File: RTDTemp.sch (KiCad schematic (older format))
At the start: 100 parts, among them J1 Conn_01x02, J10 Conn_01x02, J11 Conn_01x02, J2 Conn_01x02, J3 Conn_01x02, J4 CAN_In, J5 CAN_Out, J6 Conn_01x02, J7 Conn_01x02, J8 Conn_01x02, J9 Conn_01x02, U1 INA21x, U10 INA21x, U11 INA21x, U12 INA21x, U2 Nucleo_L432KC, U3 PDS1-Sx-Sx, U4 INA21x, U5 ADM3055E, U6 INA21x, U7 CDSOT23-T24CAN, U8 INA21x, U9 INA21x

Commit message: replacedOpAmpswithMaximChip
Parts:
- removed C1, C17, C18, C19, C2, C3, C4, C5: .1u, Capacitor_SMD:C_0805_2012Metric, symbol Device:C
- removed J1, J10, J2, J3, J6, J7, J8, J9: Conn_01x02, Connector_Molex:Molex_Micro-Fit_3.0_43650-0200_1x02_P3.00mm_Horizontal, symbol Connector_Generic:Conn_01x02
- removed R1, R11, R17, R18, R2, R23, R24, R27, R28, R3, R30, R31, R4, R5, R6, R8: 3.3k, Resistor_SMD:R_0805_2012Metric, symbol Device:R
- removed R12, R13, R15, R16, R19, R26, R29, R32: 100, Resistor_SMD:R_0805_2012Metric, symbol Device:R
- removed TP1, TP2, TP3, TP4, TP5, TP6, TP7, TP8: TestPoint, TestPoint:TestPoint_Keystone_5005-5009_Compact, symbol Connector:TestPoint
- removed U1, U10, U11, U12, U4, U6, U8, U9: INA21x, UTSVT_ICs:SOIC-6_1.40x2.15mm_Pitch0.65mm, symbol RTDTemp-rescue:INA21x-MPPT-rescue
- added C1, C17, C18, C19, C2, C20, C23, C24, C25, C26, C29, C3, C30, C31, C32, C4: 100nF, Capacitor_SMD:C_0805_2012Metric, symbol Device:C_Small
- added C21, C22, C27, C28, C33, C34, C5, C8: Ci, Capacitor_SMD:C_0805_2012Metric, symbol Device:C_Small
- added J1, J10, J2, J3, J6, J7, J8, J9: Conn_01x04, Connector_Molex:Molex_Micro-Fit_3.0_43650-0415_1x04_P3.00mm_Vertical, symbol Connector_Generic:Conn_01x04
- added R1, R2, R3, R4, R5, R6, R7, R8: 400, Resistor_SMD:R_0805_2012Metric, symbol Device:R_Small
- added U1, U10, U11, U12, U4, U6, U8, U9: MAX31865xAP, Package_SO:SSOP-20_5.3x7.2mm_P0.65mm, symbol Sensor_Temperature:MAX31865xAP
- U3: symbol utsvt-power-regulators:PDS1-Sx-Sx -> RTDTemp-rescue:PDS1-Sx-Sx-utsvt-power-regulators
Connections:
- net labels added: +3V3, CLK, CS_0, CS_1, CS_2, CS_3, CS_4, CS_5, CS_6, CS_7, DRDY, SDI, SDO
- net labels removed: RTD0, RTD1, RTD2, RTD3, RTD4, RTD5, RTD6, RTD7
- wire segments 309 -> 389
- no-connect marks 19 -> 15
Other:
- moved on the sheet: C10, C11, C12, C13, C14, C15, C16, C6, C7, C9, H1, H2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

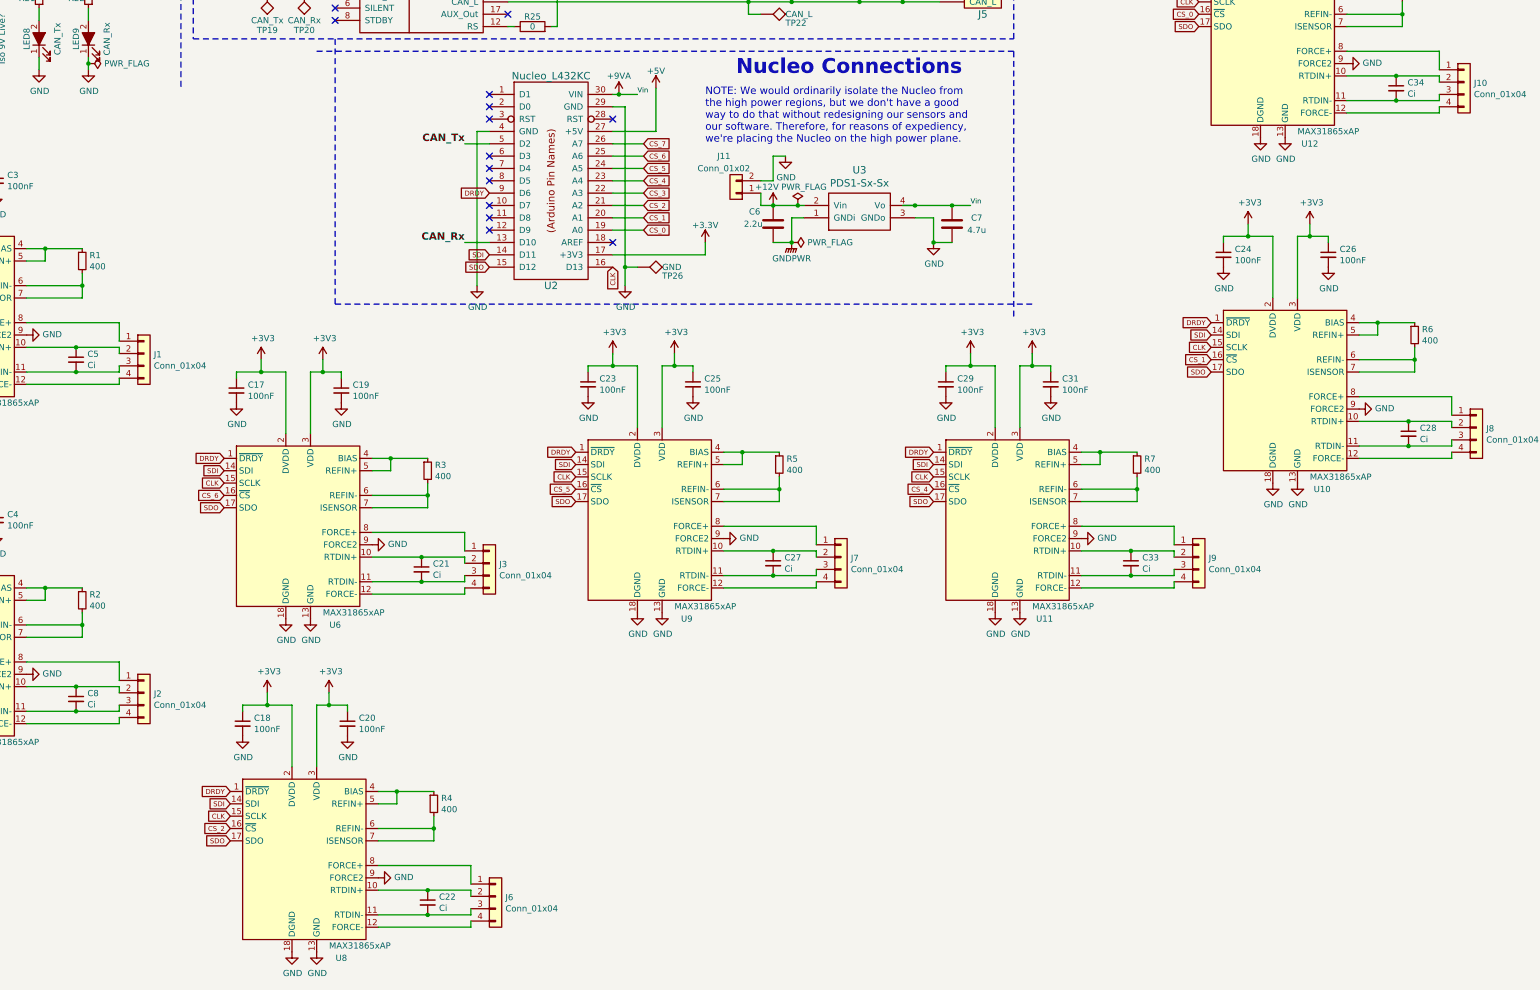
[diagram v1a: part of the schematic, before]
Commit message: Started RTD board layout update
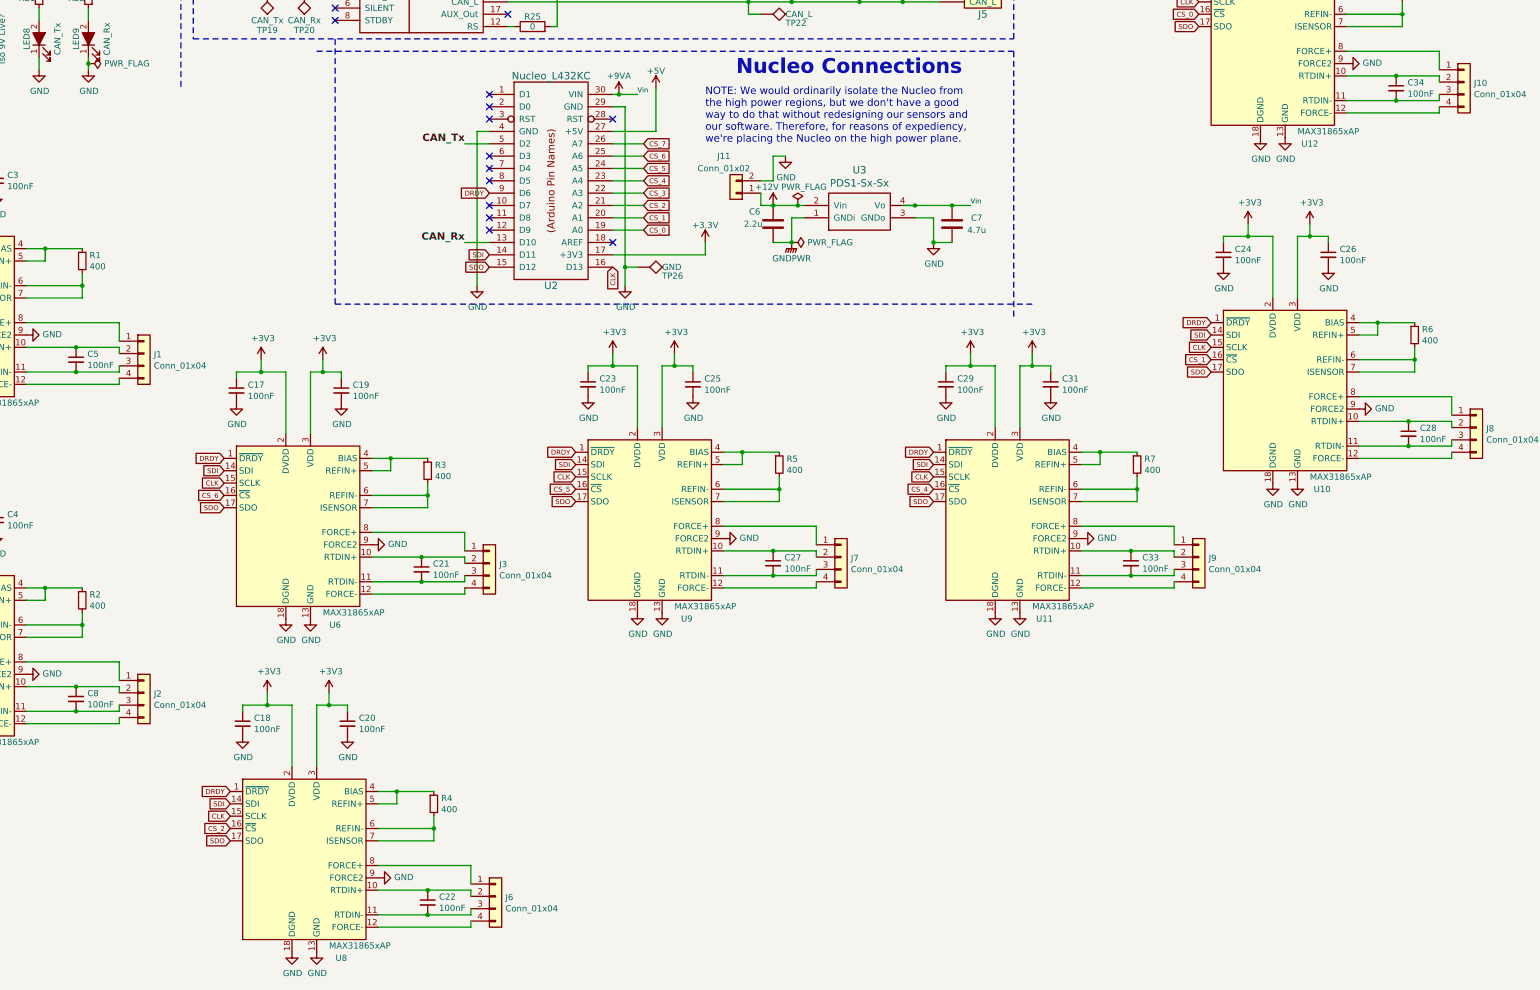
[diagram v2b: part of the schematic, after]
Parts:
- C21, C22, C27, C28, C33, C34, C5, C8: value Ci -> 100nF
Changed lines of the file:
@@
 Wire Wire Line
 	1000 3200 1000 3250
-$Comp
-L Device:C_Small C5
-U 1 1 5FC107A3
-P 2500 4800
-F 0 "C5" H 2592 4846 50  0000 L CNN
-F 1 "Ci" H 2592 4755 50  0000 L CNN
-F 2 "Capacitor_SMD:C_0805_2012Metric" H 2500 4800 50  0001 C CNN
-F 3 "~" H 2500 4800 50  0001 C CNN
-	1    2500 4800
-	1    0    0    -1
-$EndComp
 Wire Wire Line
 	2100 4700 2500 4700
@@
 P 5300 6500
 F 0 "C21" H 5392 6546 50  0000 L CNN
-F 1 "Ci" H 5392 6455 50  0000 L CNN
+F 1 "100nF" H 5392 6455 50  0000 L CNN
 F 2 "Capacitor_SMD:C_0805_2012Metric" H 5300 6500 50  0001 C CNN
 F 3 "~" H 5300 6500 50  0001 C CNN
@@
 P 8150 6450
 F 0 "C27" H 8242 6496 50  0000 L CNN
-F 1 "Ci" H 8242 6405 50  0000 L CNN
+F 1 "100nF" H 8242 6405 50  0000 L CNN
 F 2 "Capacitor_SMD:C_0805_2012Metric" H 8150 6450 50  0001 C CNN
 F 3 "~" H 8150 6450 50  0001 C CNN
@@
 P 11050 6450
 F 0 "C33" H 11142 6496 50  0000 L CNN
-F 1 "Ci" H 11142 6405 50  0000 L CNN
+F 1 "100nF" H 11142 6405 50  0000 L CNN
 F 2 "Capacitor_SMD:C_0805_2012Metric" H 11050 6450 50  0001 C CNN
 F 3 "~" H 11050 6450 50  0001 C CNN
@@
 P 2500 7550
 F 0 "C8" H 2592 7596 50  0000 L CNN
-F 1 "Ci" H 2592 7505 50  0000 L CNN
+F 1 "100nF" H 2592 7505 50  0000 L CNN
 F 2 "Capacitor_SMD:C_0805_2012Metric" H 2500 7550 50  0001 C CNN
 F 3 "~" H 2500 7550 50  0001 C CNN
@@
 P 5350 9200
 F 0 "C22" H 5442 9246 50  0000 L CNN
-F 1 "Ci" H 5442 9155 50  0000 L CNN
+F 1 "100nF" H 5442 9155 50  0000 L CNN
 F 2 "Capacitor_SMD:C_0805_2012Metric" H 5350 9200 50  0001 C CNN
 F 3 "~" H 5350 9200 50  0001 C CNN
@@
 P 13300 5400
 F 0 "C28" H 13392 5446 50  0000 L CNN
-F 1 "Ci" H 13392 5355 50  0000 L CNN
+F 1 "100nF" H 13392 5355 50  0000 L CNN
 F 2 "Capacitor_SMD:C_0805_2012Metric" H 13300 5400 50  0001 C CNN
 F 3 "~" H 13300 5400 50  0001 C CNN
@@
 P 13200 2600
 F 0 "C34" H 13292 2646 50  0000 L CNN
-F 1 "Ci" H 13292 2555 50  0000 L CNN
+F 1 "100nF" H 13292 2555 50  0000 L CNN
 F 2 "Capacitor_SMD:C_0805_2012Metric" H 13200 2600 50  0001 C CNN
 F 3 "~" H 13200 2600 50  0001 C CNN
@@
 	-1   0    0    -1
 $EndComp
+$Comp
+L Device:C_Small C5
+U 1 1 5FC107A3
+P 2500 4800
+F 0 "C5" H 2592 4846 50  0000 L CNN
+F 1 "100nF" H 2592 4755 50  0000 L CNN
+F 2 "Capacitor_SMD:C_0805_2012Metric" H 2500 4800 50  0001 C CNN
+F 3 "~" H 2500 4800 50  0001 C CNN
+	1    2500 4800
+	1    0    0    -1
+$EndComp
 $EndSCHEMATC

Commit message: reset references for rtd specific components, preliminary layout of half of the RTD subcircuits
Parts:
- removed C1, C17, C18, C19, C2, C20, C21, C22, C23, C25, C27, C29, C3, C31, C33, C4, C5, C8: 100nF, Capacitor_SMD:C_0805_2012Metric, symbol Device:C_Small
- removed J1, J2, J3, J6, J7, J9: Conn_01x04, Connector_Molex:Molex_Micro-Fit_3.0_43650-0415_1x04_P3.00mm_Vertical, symbol Connector_Generic:Conn_01x04
- removed R1, R2, R3, R4, R5, R7: 400, Resistor_SMD:R_0805_2012Metric, symbol Device:R_Small
- removed U1, U11, U4, U6, U8, U9: MAX31865xAP, Package_SO:SSOP-20_5.3x7.2mm_P0.65mm, symbol Sensor_Temperature:MAX31865xAP
- added RTD2_C0, RTD2_C1, RTD2_C2, RTD3_C0, RTD3_C1, RTD3_C2, RTD4_C0, RTD4_C1, RTD4_C2, RTD5_C0, RTD5_C1, RTD5_C2, RTD6_C0, RTD6_C1, RTD6_C2, RTD7_C0, RTD7_C1, RTD7_C2: 100nF, Capacitor_SMD:C_0805_2012Metric, symbol Device:C_Small
- added RTD2_J0, RTD3_J0, RTD4_J0, RTD5_J0, RTD6_J0, RTD7_J0: Conn_01x04, Connector_Molex:Molex_Micro-Fit_3.0_43650-0415_1x04_P3.00mm_Vertical, symbol Connector_Generic:Conn_01x04
- added RTD2_R0, RTD3_R0, RTD4_R0, RTD5_R0, RTD6_R0, RTD7_R0: 400, Resistor_SMD:R_0805_2012Metric, symbol Device:R_Small
- added RTD2_U0, RTD3_U0, RTD4_U0, RTD5_U0, RTD6_U0, RTD7_U0: MAX31865xAP, Package_SO:SSOP-20_5.3x7.2mm_P0.65mm, symbol Sensor_Temperature:MAX31865xAP
- renumbered C30 to RTD0_C0, C32 to RTD0_C1, C34 to RTD0_C2, J10 to RTD0_J0, R8 to RTD0_R0, U12 to RTD0_U0, C24 to RTD1_C0, C26 to RTD1_C1, C28 to RTD1_C2, J8 to RTD1_J0, R6 to RTD1_R0, U10 to RTD1_U0
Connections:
- net +3V3: now also RTD2_C0.1, RTD2_C1.1, RTD2_U0.2 (DVDD), RTD2_U0.3 (VDD), RTD3_C0.1, RTD3_C1.1, RTD3_U0.2 (DVDD), RTD3_U0.3 (VDD), RTD4_C0.1, RTD4_C1.1, RTD4_U0.2 (DVDD), RTD4_U0.3 (VDD), RTD5_C0.1, RTD5_C1.1, RTD5_U0.2 (DVDD), RTD5_U0.3 (VDD), RTD6_C0.1, RTD6_C1.1, RTD6_U0.2 (DVDD), RTD6_U0.3 (VDD), RTD7_C0.1, RTD7_C1.1, RTD7_U0.2 (DVDD), RTD7_U0.3 (VDD)
- net CLK: now also RTD2_U0.15 (SCLK), RTD3_U0.15 (SCLK), RTD4_U0.15 (SCLK), RTD5_U0.15 (SCLK), RTD6_U0.15 (SCLK), RTD7_U0.15 (SCLK)
- net CS_2: now also RTD2_U0.16 (~CS)
- net CS_3: now also RTD3_U0.16 (~CS)
- net CS_4: now also RTD4_U0.16 (~CS)
- net CS_5: now also RTD5_U0.16 (~CS)
- net CS_6: now also RTD6_U0.16 (~CS)
- net CS_7: now also RTD7_U0.16 (~CS)
- net DRDY: now also RTD2_U0.1 (~DRDY), RTD3_U0.1 (~DRDY), RTD4_U0.1 (~DRDY), RTD5_U0.1 (~DRDY), RTD6_U0.1 (~DRDY), RTD7_U0.1 (~DRDY)
- net GND: now also RTD2_C0.2, RTD2_C1.2, RTD2_U0.13 (GND), RTD2_U0.18 (DGND), RTD2_U0.19 (GND), RTD2_U0.9 (FORCE2), RTD3_C0.2, RTD3_C1.2, RTD3_U0.13 (GND), RTD3_U0.18 (DGND), RTD3_U0.19 (GND), RTD3_U0.9 (FORCE2), RTD4_C0.2, RTD4_C1.2, RTD4_U0.13 (GND), RTD4_U0.18 (DGND), RTD4_U0.19 (GND), RTD4_U0.9 (FORCE2), RTD5_C0.2, RTD5_C1.2, RTD5_U0.13 (GND), RTD5_U0.18 (DGND), RTD5_U0.19 (GND), RTD5_U0.9 (FORCE2), RTD6_C0.2, RTD6_C1.2, RTD6_U0.13 (GND), RTD6_U0.18 (DGND), RTD6_U0.19 (GND), RTD6_U0.9 (FORCE2), RTD7_C0.2, RTD7_C1.2, RTD7_U0.13 (GND), RTD7_U0.18 (DGND), RTD7_U0.19 (GND), RTD7_U0.9 (FORCE2)
- net SDI: now also RTD2_U0.14 (SDI), RTD3_U0.14 (SDI), RTD4_U0.14 (SDI), RTD5_U0.14 (SDI), RTD6_U0.14 (SDI), RTD7_U0.14 (SDI)
- net SDO: now also RTD2_U0.17 (SDO), RTD3_U0.17 (SDO), RTD4_U0.17 (SDO), RTD5_U0.17 (SDO), RTD6_U0.17 (SDO), RTD7_U0.17 (SDO)
- new net: RTD3_R0.1, RTD3_U0.4 (BIAS), RTD3_U0.5 (REFIN+)
- new net: RTD3_R0.2, RTD3_U0.6 (REFIN-), RTD3_U0.7 (ISENSOR)
- new net: RTD3_C2.1, RTD3_J0.2 (Pin_2), RTD3_U0.10 (RTDIN+)
- new net: RTD3_C2.2, RTD3_J0.3 (Pin_3), RTD3_U0.11 (RTDIN-)
- new net: RTD3_J0.1 (Pin_1), RTD3_U0.8 (FORCE+)
- new net: RTD3_J0.4 (Pin_4), RTD3_U0.12 (FORCE-)
- new net: RTD4_R0.1, RTD4_U0.4 (BIAS), RTD4_U0.5 (REFIN+)
- new net: RTD4_R0.2, RTD4_U0.6 (REFIN-), RTD4_U0.7 (ISENSOR)
- new net: RTD4_C2.1, RTD4_J0.2 (Pin_2), RTD4_U0.10 (RTDIN+)
- new net: RTD4_C2.2, RTD4_J0.3 (Pin_3), RTD4_U0.11 (RTDIN-)
- new net: RTD4_J0.1 (Pin_1), RTD4_U0.8 (FORCE+)
- new net: RTD4_J0.4 (Pin_4), RTD4_U0.12 (FORCE-)
- new net: RTD5_C2.1, RTD5_J0.2 (Pin_2), RTD5_U0.10 (RTDIN+)
- new net: RTD5_C2.2, RTD5_J0.3 (Pin_3), RTD5_U0.11 (RTDIN-)
- new net: RTD5_J0.4 (Pin_4), RTD5_U0.12 (FORCE-)
- new net: RTD5_R0.1, RTD5_U0.4 (BIAS), RTD5_U0.5 (REFIN+)
- new net: RTD5_R0.2, RTD5_U0.6 (REFIN-), RTD5_U0.7 (ISENSOR)
- new net: RTD5_J0.1 (Pin_1), RTD5_U0.8 (FORCE+)
- new net: RTD6_C2.1, RTD6_J0.2 (Pin_2), RTD6_U0.10 (RTDIN+)
- new net: RTD6_C2.2, RTD6_J0.3 (Pin_3), RTD6_U0.11 (RTDIN-)
- new net: RTD6_J0.4 (Pin_4), RTD6_U0.12 (FORCE-)
- new net: RTD6_R0.1, RTD6_U0.4 (BIAS), RTD6_U0.5 (REFIN+)
- new net: RTD6_R0.2, RTD6_U0.6 (REFIN-), RTD6_U0.7 (ISENSOR)
- new net: RTD6_J0.1 (Pin_1), RTD6_U0.8 (FORCE+)
- new net: RTD2_C2.1, RTD2_J0.2 (Pin_2), RTD2_U0.10 (RTDIN+)
- new net: RTD2_C2.2, RTD2_J0.3 (Pin_3), RTD2_U0.11 (RTDIN-)
- new net: RTD2_J0.4 (Pin_4), RTD2_U0.12 (FORCE-)
- new net: RTD2_R0.1, RTD2_U0.4 (BIAS), RTD2_U0.5 (REFIN+)
- new net: RTD2_R0.2, RTD2_U0.6 (REFIN-), RTD2_U0.7 (ISENSOR)
- new net: RTD2_J0.1 (Pin_1), RTD2_U0.8 (FORCE+)
- new net: RTD7_C2.1, RTD7_J0.2 (Pin_2), RTD7_U0.10 (RTDIN+)
- new net: RTD7_C2.2, RTD7_J0.3 (Pin_3), RTD7_U0.11 (RTDIN-)
- new net: RTD7_J0.4 (Pin_4), RTD7_U0.12 (FORCE-)
- new net: RTD7_R0.1, RTD7_U0.4 (BIAS), RTD7_U0.5 (REFIN+)
- new net: RTD7_R0.2, RTD7_U0.6 (REFIN-), RTD7_U0.7 (ISENSOR)
- new net: RTD7_J0.1 (Pin_1), RTD7_U0.8 (FORCE+)
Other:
- note added: "For a maximum of 8, we tie SPI SDI/SDO/SCLK/DRDY for all of them\nand use the CS pin for controlling which ones get to send across data\non the bus."
- note added: "RTD Sensors"
- moved on the sheet: C10, C11, C12, C13, C14, C15, C16, C6, C7, C9, H1, H2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
